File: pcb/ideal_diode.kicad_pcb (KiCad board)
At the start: 2 copper layers, 34 x 25 mm, 76 parts, among them P1 CONN_01X03, Q1 BSC028N06NS, Q2 BSC028N06NS, U1 LTC4359

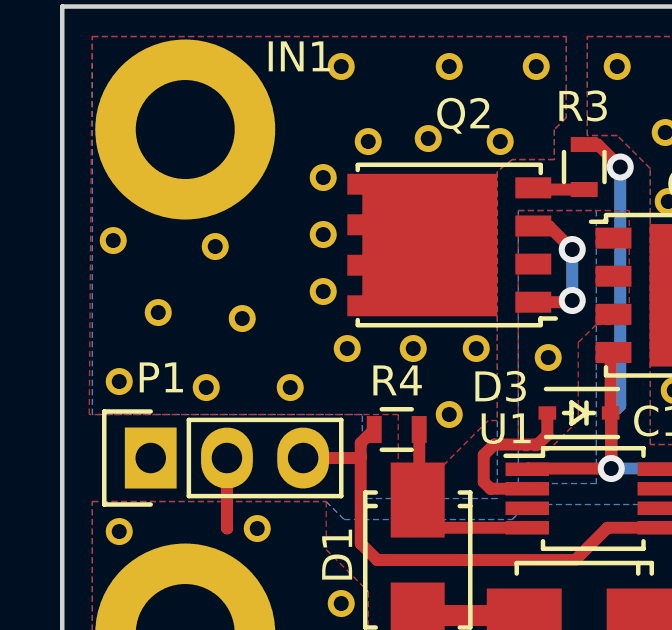
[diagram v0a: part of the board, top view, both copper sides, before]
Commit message: setting license as CERN OHL updating titleblocks ready for 1.0 release, added silkscreen ID & version. changed from 4V-70V to 5V-60V to reflect design capabilities changed R1 from 1k to 3k6 & removed text note added description, manufacturer, part number & supplier info for all RS parts added TODO text doc
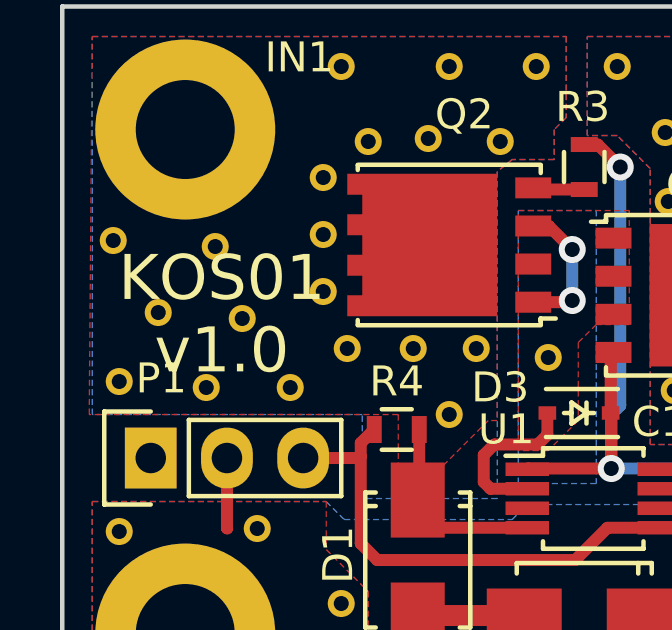
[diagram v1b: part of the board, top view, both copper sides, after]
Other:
- board text added: "KOS01 v1.0"
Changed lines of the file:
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@@
-(kicad_pcb (version 4) (host pcbnew 4.0.1-stable)
+(kicad_pcb (version 4) (host pcbnew 4.0.4-stable)
   (general
     (links 100)
     (no_connects 0)
-    (area 114.091667 85.472619 182.458334 122.775)
+    (area 114.166667 85.547619 182.383334 122.875)
     (thickness 1.6)
-    (drawings 8)
+    (drawings 9)
     (tracks 64)
     (zones 0)
@@
   (page A4)
   (title_block
-    (title "20A Ideal Diode LTC4359 4V-70V")
-    (date 2016-01-22)
-    (rev 0.9)
+    (title "20A Ideal Diode LTC4359 5V-60V")
+    (date 2016-12-10)
+    (rev 1.0)
   )
   (layers
@@
     (solder_mask_min_width 0.1)
     (aux_axis_origin 129.3 113.8)
-    (visible_elements 7FFFFFFF)
+    (visible_elements 7FFFFFDF)
     (pcbplotparams
       (layerselection 0x010e8_80000001)
@@
       (net 8 /SOURCE))
   )
+  (gr_text "KOS01\nv1.0" (at 134.62 99.06) (layer F.SilkS)
+    (effects (font (size 1.5 1.5) (thickness 0.3)))
+  )
   (gr_line (start 130.3 112.8) (end 162.3 112.8) (angle 90) (layer Margin) (width 0.2))

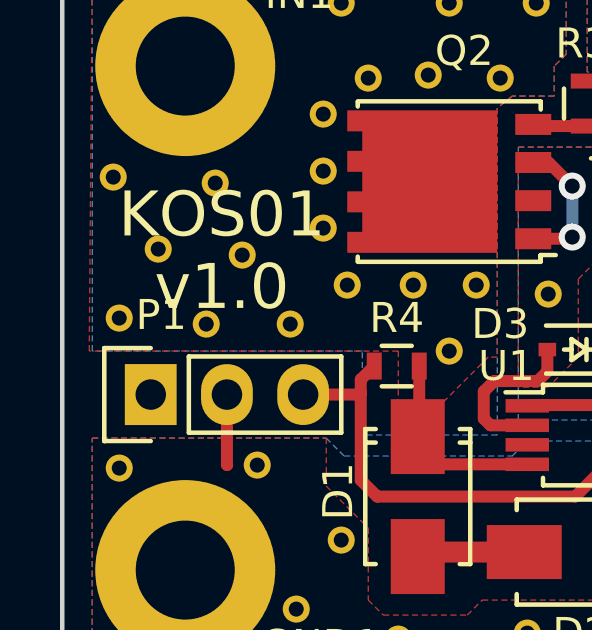
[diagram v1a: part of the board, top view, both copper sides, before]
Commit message: last few changes for v1.0 Release Added part info for commodity R's and P1 Re-exported BOM and PCB data after minor changes since proto v0.9 added MPNs to one click BOM Updated readme & TODO, dates & version info etc moved drill files to /gerbers folder
Signed-off-by: Kevin Bibby <kevin@inanecoding.co.uk>
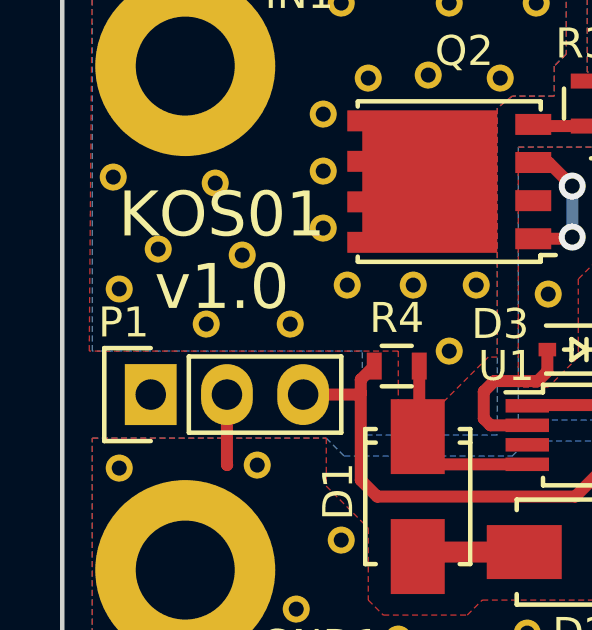
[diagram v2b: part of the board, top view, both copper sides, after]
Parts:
- R1: value 1k -> 3k6
- moved REF** 0.97 mm to (131.2, 100.3)
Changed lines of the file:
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@@
     (links 100)
     (no_connects 0)
-    (area 114.166667 85.547619 182.383334 122.875)
+    (area 129.224999 88.724999 163.375001 113.875001)
     (thickness 1.6)
     (drawings 9)
@@
   (title_block
     (title "20A Ideal Diode LTC4359 5V-60V")
-    (date 2016-12-10)
+    (date 2017-02-25)
     (rev 1.0)
   )
   (layers
     (0 F.Cu signal)
-    (31 B.Cu signal hide)
+    (31 B.Cu signal)
     (33 F.Adhes user)
     (35 F.Paste user)
@@
   )
   (module _kb_footprint:via_0-9_0-5mm (layer F.Cu)
-    (at 131.2 101.3)
+    (at 131.2 100.33)
     (fp_text reference REF** (at 0 0.5) (layer F.SilkS) hide
       (effects (font (size 1 1) (thickness 0.15)))
@@
       (effects (font (size 1 1) (thickness 0.15)))
     )
-    (fp_text value 1k (at 0.9 -14.55 270) (layer F.Fab)
+    (fp_text value 3k6 (at 0.9 -14.55 270) (layer F.Fab)
       (effects (font (size 1 1) (thickness 0.15)))
     )
@@
     (descr "Through hole pin header")
     (tags "pin header")
-    (fp_text reference P1 (at 2.65 0.35 180) (layer F.SilkS)
-      (effects (font (size 1 1) (thickness 0.15)))
-    )
+    (fp_text reference P1 (at 2.4 -0.9 180) (layer F.SilkS)
+      (effects (font (size 1 1) (thickness 0.15)))
+    )

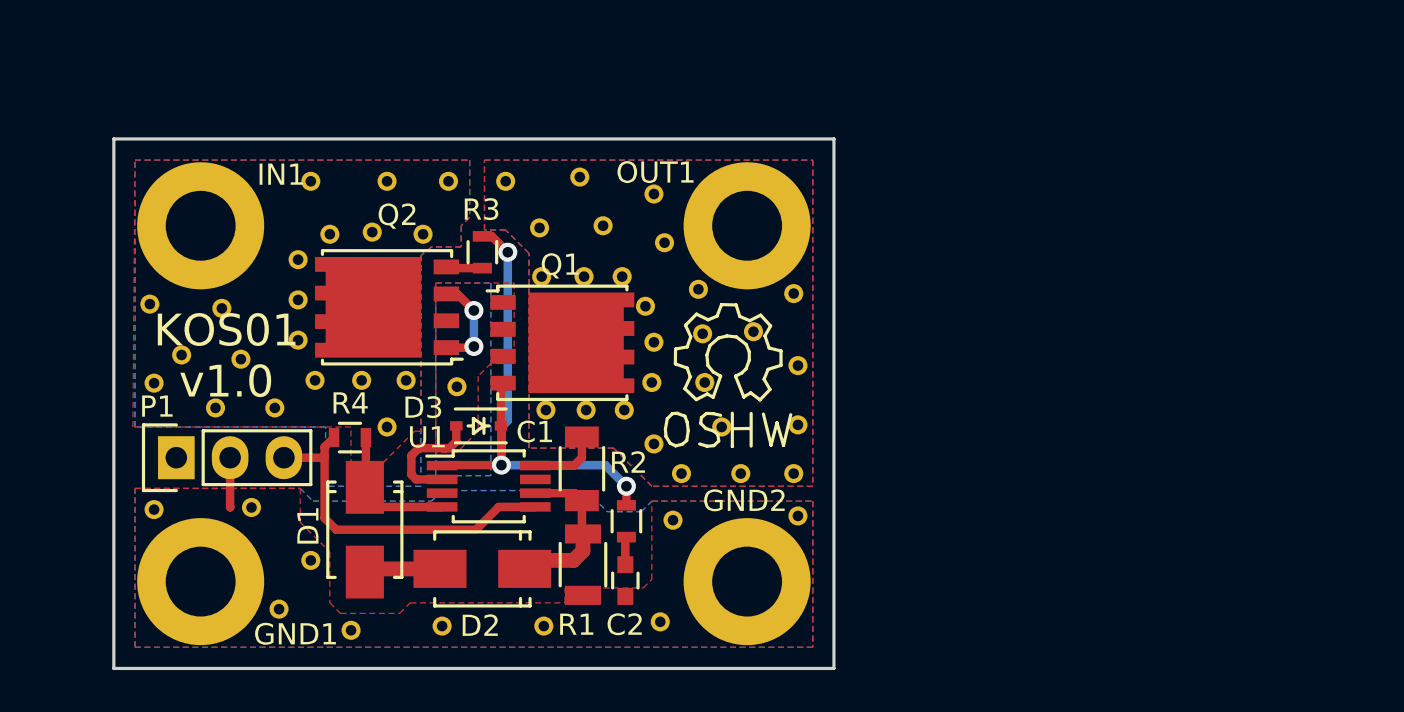
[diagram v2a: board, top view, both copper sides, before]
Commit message: moved FETs upwards & centred IN/OUT holes to FETs made PCB slightly wider added thermal relief on pads connecting to planes removed extra text from thermal via components so pcb design not cluttered
Signed-off-by: Kevin Bibby <kevin@inanecoding.co.uk>
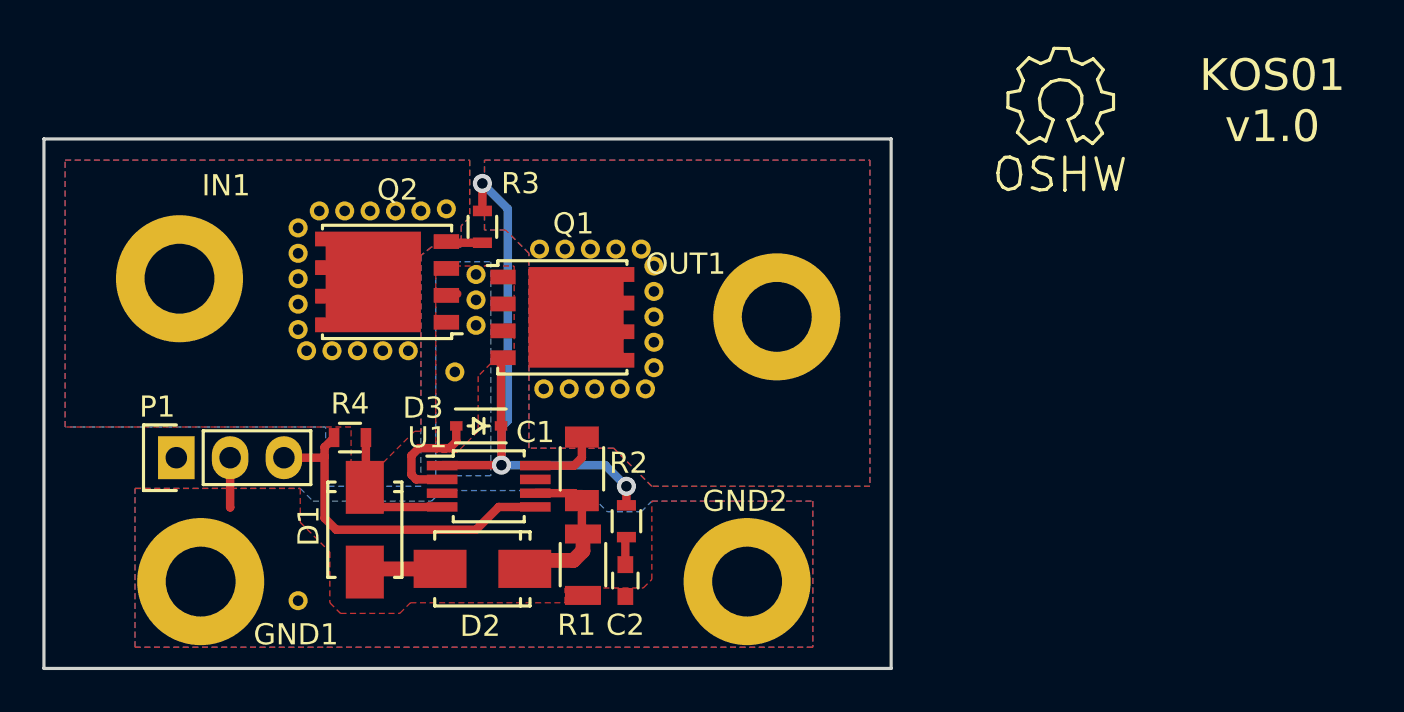
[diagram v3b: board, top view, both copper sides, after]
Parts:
- removed REF** (x57): via_0-9_0-5mm, _kb_footprint:via_0-9_0-5mm
- added ?: , _kb_footprint:via_0-9_0-5mm, F.Cu at (145.4, 99.8)
- added ?: , _kb_footprint:via_0-9_0-5mm, F.Cu at (138.0, 96.6)
- added ?: , _kb_footprint:via_0-9_0-5mm, F.Cu at (138.0, 95.4)
- added ?: , _kb_footprint:via_0-9_0-5mm, F.Cu at (138.0, 94.2)
- added ?: , _kb_footprint:via_0-9_0-5mm, F.Cu at (138.0, 93.0)
- added ?: , _kb_footprint:via_0-9_0-5mm, F.Cu at (139.0, 92.2)
- added ?: , _kb_footprint:via_0-9_0-5mm, F.Cu at (140.2, 92.2)
- added ?: , _kb_footprint:via_0-9_0-5mm, F.Cu at (141.4, 92.2)
- added ?: , _kb_footprint:via_0-9_0-5mm, F.Cu at (142.6, 92.2)
- added ?: , _kb_footprint:via_0-9_0-5mm, F.Cu at (143.8, 92.2)
- added ?: , _kb_footprint:via_0-9_0-5mm, F.Cu at (149.6, 100.6)
- added ?: , _kb_footprint:via_0-9_0-5mm, F.Cu at (146.4, 97.6)
- added ?: , _kb_footprint:via_0-9_0-5mm, F.Cu at (150.8, 100.6)
- added ?: , _kb_footprint:via_0-9_0-5mm, F.Cu at (154.2, 94.0)
- added ?: , _kb_footprint:via_0-9_0-5mm, F.Cu at (154.4, 100.6)
- added ?: , _kb_footprint:via_0-9_0-5mm, F.Cu at (146.4, 95.2)
- added ?: , _kb_footprint:via_0-9_0-5mm, F.Cu at (145.0, 92.1)
- added ?: , _kb_footprint:via_0-9_0-5mm, F.Cu at (138.0, 110.6)
- added ?: , _kb_footprint:via_0-9_0-5mm, F.Cu at (152.0, 100.6)
- added ?: , _kb_footprint:via_0-9_0-5mm, F.Cu at (153.2, 100.6)
- added ?: , _kb_footprint:via_0-9_0-5mm, F.Cu at (154.8, 99.6)
- added ?: , _kb_footprint:via_0-9_0-5mm, F.Cu at (154.8, 98.4)
- added ?: , _kb_footprint:via_0-9_0-5mm, F.Cu at (146.4, 96.4)
- added ?: , _kb_footprint:via_0-9_0-5mm, F.Cu at (154.8, 97.2)
- added ?: , _kb_footprint:via_0-9_0-5mm, F.Cu at (154.8, 96.0)
- added ?: , _kb_footprint:via_0-9_0-5mm, F.Cu at (154.8, 94.8)
- added ?: , _kb_footprint:via_0-9_0-5mm, F.Cu at (153.0, 94.0)
- added ?: , _kb_footprint:via_0-9_0-5mm, F.Cu at (151.8, 94.0)
- added ?: , _kb_footprint:via_0-9_0-5mm, F.Cu at (150.6, 94.0)
- added ?: , _kb_footprint:via_0-9_0-5mm, F.Cu at (138.4, 98.8)
- added ?: , _kb_footprint:via_0-9_0-5mm, F.Cu at (139.6, 98.8)
- added ?: , _kb_footprint:via_0-9_0-5mm, F.Cu at (140.8, 98.8)
- added ?: , _kb_footprint:via_0-9_0-5mm, F.Cu at (142.0, 98.8)
- added ?: , _kb_footprint:via_0-9_0-5mm, F.Cu at (143.2, 98.8)
- added ?: , _kb_footprint:via_0-9_0-5mm, F.Cu at (138.0, 97.8)
- ?: renamed from REF**; value via_0-9_0-5mm -> (none)
- moved ? 19.8 mm to (174.0, 87.0)
- moved OUT1 4.52 mm to (160.6, 97.2)
- moved ? 4.11 mm to (149.4, 94.0)
- moved IN1 2.69 mm to (132.4, 95.4)
- moved Q1 1.20 mm to (150.5, 97.2)
- moved Q2 1.20 mm to (142.2, 95.5)
- moved R3 1.20 mm to (146.7, 93.0)
- renumbered REF** to ?
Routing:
- net /GATE: track 25.6 -> 30.4 mm
- net /SOURCE: track 10.2 -> 6.16 mm, vias 2 -> 0
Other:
- board size 34 x 25 mm -> 40 x 25 mm
- net class Default: clearance 0.15 -> 0.2
- rule trace_clearance: 0.15 -> 0.2
